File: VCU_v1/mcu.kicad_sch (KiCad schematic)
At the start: 16 parts, among them SW1 SW_Push, U3 STM32H723ZGT6, Y1 16 MHz, Y2 32.768 kHz

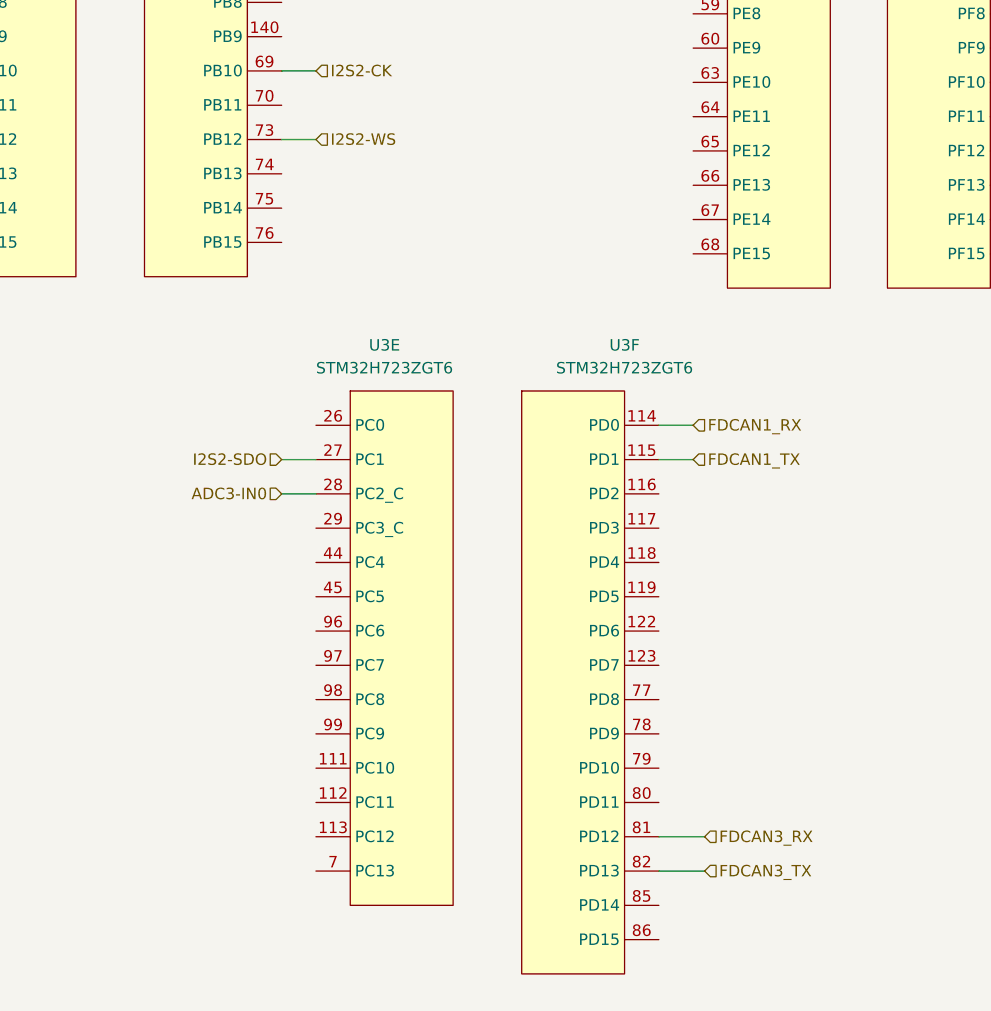
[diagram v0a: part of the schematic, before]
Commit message: added rpp, pedal buffer/low pass, can transceivers, began connector pinout
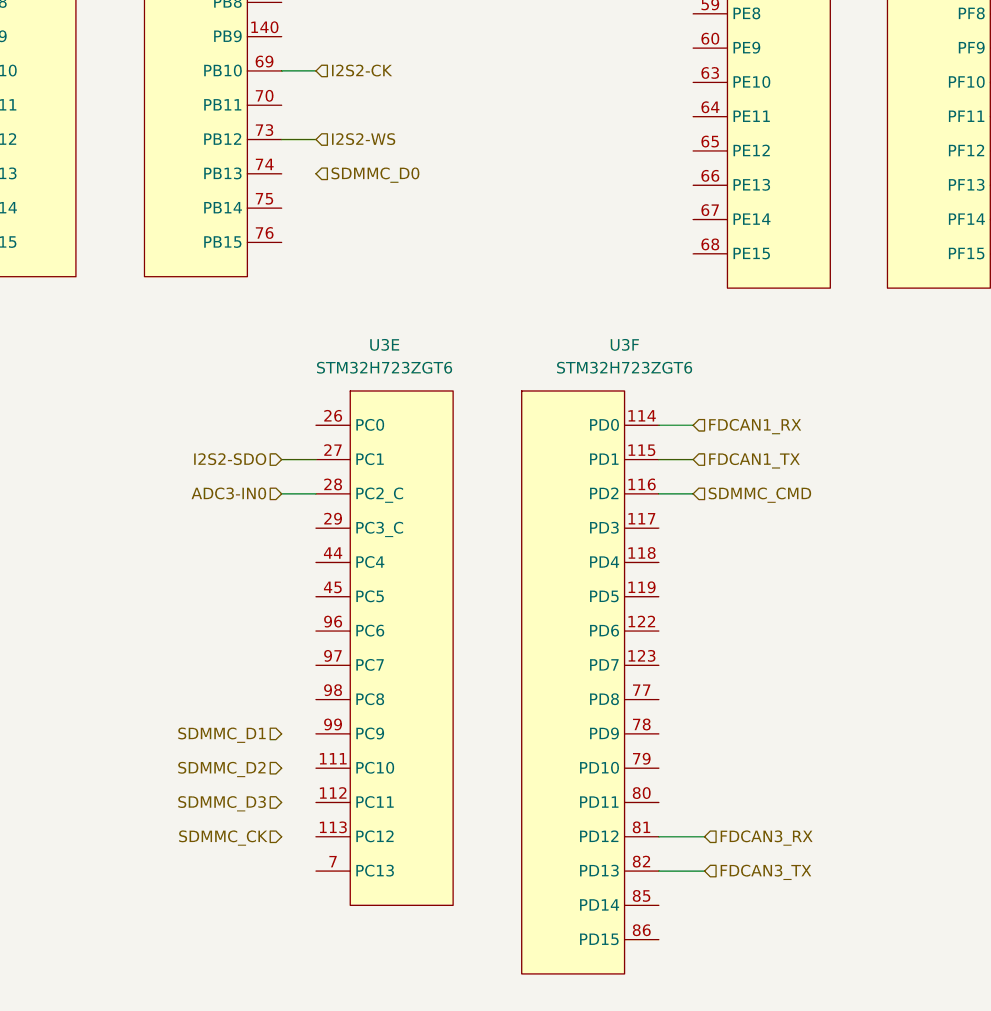
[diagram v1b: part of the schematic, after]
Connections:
- net SDMMC_CMD: now reaches U3.116 (PD2)
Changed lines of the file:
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@@
+	(wire
+		(pts
+			(xy 209.55 110.49) (xy 213.36 110.49)
+		)
+		(stroke
+			(width 0)
+			(type default)
+		)
+	)
 	(wire
 		(pts
@@
 		)
 	)
+	(hierarchical_label "SDMMC_D2"
+		(shape input)
+		(at 167.64 140.97 180)
+		(effects
+			(font
+				(size 1.27 1.27)
+			)
+			(justify right)
+		)
+	)
 	(hierarchical_label "I2S2-SDO"
 		(shape input)
@@
 		)
 	)
+	(hierarchical_label "SDMMC_D0"
+		(shape input)
+		(at 171.45 74.93 0)
+		(effects
+			(font
+				(size 1.27 1.27)
+			)
+			(justify left)
+		)
+	)
 	(hierarchical_label "DEBUG_SWCLK"
 		(shape input)
@@
 		)
 	)
+	(hierarchical_label "SDMMC_D1"
+		(shape input)
+		(at 167.64 137.16 180)
+		(effects
+			(font
+				(size 1.27 1.27)
+			)
+			(justify right)
+		)
+	)
 	(hierarchical_label "DEBUG_SWDIO"
 		(shape input)
@@
 		)
 	)
+	(hierarchical_label "SDMMC_D3"
+		(shape input)
+		(at 167.64 144.78 180)
+		(effects
+			(font
+				(size 1.27 1.27)
+			)
+			(justify right)
+		)
+	)
 	(hierarchical_label "FDCAN1_RX"
 		(shape input)
@@
 		)
 	)
+	(hierarchical_label "SDMMC_CK"
+		(shape input)
+		(at 167.64 148.59 180)
+		(effects
+			(font
+				(size 1.27 1.27)
+			)
+			(justify right)
+		)
+	)
 	(hierarchical_label "I2S2-CK"
 		(shape input)
@@
 		(effects
 			(font
+				(size 1.27 1.27)
+			)
+			(justify left)
+		)
+	)
+	(hierarchical_label "SDMMC_CMD"
+		(shape input)
+		(at 213.36 110.49 0)
+		(effects
+			(font

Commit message: p dih r
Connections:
- net GPIO_IN_E7: now reaches U3.58 (PE7)
- net GPIO_IN_E8: now reaches U3.59 (PE8)
- net GPIO_IN_E9: now reaches U3.60 (PE9)
- net GPIO_OUT_E10: now reaches U3.63 (PE10)
- net GPIO_OUT_E11: now reaches U3.64 (PE11)
- net GPIO_OUT_E12: now reaches U3.65 (PE12)
- net GPIO_OUT_E13: now reaches U3.66 (PE13)
- net GPIO_OUT_E14: now reaches U3.67 (PE14)
- net GPIO_OUT_E15: now reaches U3.68 (PE15)
- net GPIO_IN_F13: now reaches U3.53 (PF13)
- net GPIO_IN_F14: now reaches U3.54 (PF14)
- net GPIO_IN_F15: now reaches U3.55 (PF15)
- net GPIO_IN_G0: now reaches U3.56 (PG0)
- net GPIO_IN_G1: now reaches U3.57 (PG1)

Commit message: left to do before layout: wire DRS/Debug LEDs to connector, add BRUHbus ports
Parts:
- added C62, C69, C70, C71, C72, C73, C74, C75, C76, C77, C78, C79, C80, C81: 100n, Capacitor_SMD:C_0603_1608Metric_Pad1.08x0.95mm_HandSolder, symbol BFR Capacitors:06035C104KAT2A
- added J2: NUCLEO CONNECTOR LEFT, symbol Connector_Generic:Conn_02x35_Odd_Even
- added J3: NUCLEO CONNECTOR RIGHT, symbol Connector_Generic:Conn_02x35_Odd_Even
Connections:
- net +3.3V: now also C62.2, C69.2, C70.2, C71.2, C72.2, C73.2, C74.2, C75.2, C76.2, C77.2, C78.2, C79.2, C80.2, C81.2
- net ADC3-IN0: now also J2.35 (Pin_35)
- net ADC3-IN6: now also J3.42 (Pin_42)
- net ADC3-IN7: now also J2.54 (Pin_54)
- net ADC3-IN8: now also J2.9 (Pin_9)
- net ADC3-IN9: now also J3.38 (Pin_38)
- net DEBUG_SWCLK: now also J2.15 (Pin_15)
- net DEBUG_SWDIO: now also J2.13 (Pin_13)
- net DEBUG_SWO: now also J3.31 (Pin_31)
- net FDCAN1_RX: now also J2.57 (Pin_57)
- net FDCAN1_TX: now also J2.55 (Pin_55)
- net FDCAN2_RX: now also J3.29 (Pin_29)
- net FDCAN2_TX: now also J3.17 (Pin_17)
- net FDCAN3_RX: now also J3.43 (Pin_43)
- net FDCAN3_TX: now also J3.41 (Pin_41)
- net GND: now also C62.1, C69.1, C70.1, C71.1, C72.1, C73.1, C74.1, C75.1, C76.1, C77.1, C78.1, C79.1, C80.1, C81.1, J2.19 (Pin_19), J2.20 (Pin_20), J2.22 (Pin_22), J2.49 (Pin_49), J2.60 (Pin_60), J2.8 (Pin_8), J3.20 (Pin_20), J3.32 (Pin_32), J3.39 (Pin_39), J3.54 (Pin_54), J3.63 (Pin_63), J3.9 (Pin_9)
- net GPIO_IN_E7: now also J3.44 (Pin_44)
- net GPIO_IN_E8: now also J3.40 (Pin_40)
- net GPIO_IN_E9: now also J3.52 (Pin_52)
- net GPIO_IN_F13: now also J3.57 (Pin_57)
- net GPIO_IN_F14: now also J3.50 (Pin_50)
- net GPIO_IN_F15: now also J3.60 (Pin_60)
- net GPIO_IN_G0: now also J2.59 (Pin_59)
- net GPIO_IN_G1: now also J2.58 (Pin_58)
- net GPIO_OUT_E10: now also J3.47 (Pin_47)
- net GPIO_OUT_E11: now also J3.56 (Pin_56)
- net GPIO_OUT_E12: now also J3.49 (Pin_49)
- net GPIO_OUT_E13: now also J3.55 (Pin_55)
- net GPIO_OUT_E14: now also J3.51 (Pin_51)
- net GPIO_OUT_E15: now also J3.53 (Pin_53)
- net I2S2-CK: now also J3.25 (Pin_25)
- net I2S2-SDO: now also J2.36 (Pin_36)
- net I2S2-WS: now also J3.16 (Pin_16)
- net SDMMC_CK: now also U3.113 (PC12), J2.3 (Pin_3)
- net SDMMC_CMD: now also J2.4 (Pin_4)
- net SDMMC_D0: now also U3.74 (PB13), J3.30 (Pin_30)
- net SDMMC_D1: now also U3.99 (PC9), J3.1 (Pin_1)
- net SDMMC_D2: now also U3.111 (PC10), J2.1 (Pin_1)
- net SDMMC_D3: now also U3.112 (PC11), J2.2 (Pin_2)
- net SPI1_MISO: now also J3.13 (Pin_13)
- net SPI1_MOSI: now also J3.15 (Pin_15)
- net SPI1_SCK: now also J3.11 (Pin_11)
- net USB_D+: now also J3.12 (Pin_12)
- net USB_D-: now also J3.14 (Pin_14)
- net PA8: now reaches U3.100 (PA8)
- net PA8: now also J3.23 (Pin_23)
- net PA9: now reaches U3.101 (PA9)
- net PA9: now also J3.21 (Pin_21)
- net PA10: now reaches U3.102 (PA10)
- net PA10: now also J3.33 (Pin_33)
- net PA15: now reaches U3.110 (PA15)
- net PA15: now also J2.17 (Pin_17)
- net TIM2_PWM_CH1: now reaches U3.34 (PA0)
- net TIM2_PWM_CH1: now also J2.28 (Pin_28)
- net TIM2_PWM_CH2: now reaches U3.35 (PA1)
- net TIM2_PWM_CH2: now also J2.30 (Pin_30)
- net TIM2_PWM_CH3: now reaches U3.36 (PA2)
- net TIM2_PWM_CH3: now also J3.35 (Pin_35)
- net PA3: now reaches U3.37 (PA3)
- net PA3: now also J3.37 (Pin_37)
- net PA4: now reaches U3.40 (PA4)
- net PA4: now also J2.32 (Pin_32)
- net PD3: now reaches U3.117 (PD3)
- net PD3: now also J2.40 (Pin_40)
- net PD4: now reaches U3.118 (PD4)
- net PD4: now also J2.39 (Pin_39)
- net PD5: now reaches U3.119 (PD5)
- net PD5: now also J2.41 (Pin_41)
- net PD6: now reaches U3.122 (PD6)
- net PD6: now also J2.43 (Pin_43)
- net PD7: now reaches U3.123 (PD7)
- net PD7: now also J2.45 (Pin_45)
- net PD8: now reaches U3.77 (PD8)
- net PD8: now also J3.10 (Pin_10)
- net PD9: now reaches U3.78 (PD9)
- net PD9: now also J2.69 (Pin_69)
- net PD10: now reaches U3.79 (PD10)
- net PD10: now also J3.65 (Pin_65)
- net PD11: now reaches U3.80 (PD11)
- net PD11: now also J3.45 (Pin_45)
- net PD14: now reaches U3.85 (PD14)
- net PD14: now also J3.46 (Pin_46)
- net PD15: now reaches U3.86 (PD15)
- net PD15: now also J3.48 (Pin_48)
- net PE2: now reaches U3.1 (PE2)
- net PE2: now also J2.46 (Pin_46)
- net PE0: now reaches U3.141 (PE0)
- net PE0: now also J3.64 (Pin_64)
- net PE1: now reaches U3.142 (PE1)
- net PE1: now also J2.61 (Pin_61)
- net PE3: now reaches U3.2 (PE3)
- net PE3: now also J2.47 (Pin_47)
- net PE4: now reaches U3.3 (PE4)
- net PE4: now also J2.48 (Pin_48)
- net PE5: now reaches U3.4 (PE5)
- net PE5: now also J2.50 (Pin_50)
- net PE6: now reaches U3.5 (PE6)
- net PE6: now also J2.62 (Pin_62)
- net VBAT: now reaches BT1.1 (+), U3.6 (VBAT)
- net VBAT: now also J2.33 (Pin_33)
- net PF0: now reaches U3.10 (PF0)
- net PF0: now also J2.53 (Pin_53)
- net PF1: now reaches U3.11 (PF1)
- net PF1: now also J2.51 (Pin_51)
- net PF2: now reaches U3.12 (PF2)
- net PF2: now also J2.52 (Pin_52)
- net PF3: now reaches U3.13 (PF3)
- net PF3: now also J3.58 (Pin_58)
- net PF5: now reaches U3.15 (PF5)
- net PF5: now also J3.36 (Pin_36)
- net PF7: now reaches U3.19 (PF7)
- net PF7: now also J2.11 (Pin_11)
- net PF9: now reaches U3.21 (PF9)
- net PF9: now also J2.56 (Pin_56)
- net PF11: now reaches U3.49 (PF11)
- net PF11: now also J3.62 (Pin_62)
- net PF12: now reaches U3.50 (PF12)
- net PF12: now also J3.59 (Pin_59)
- net PC0: now reaches U3.26 (PC0)
- net PC0: now also J2.38 (Pin_38)
- net PC3: now reaches U3.29 (PC3_C)
- net PC3: now also J2.37 (Pin_37)
- net PC4: now reaches U3.44 (PC4)
- net PC4: now also J3.34 (Pin_34)
- net PC5: now reaches U3.45 (PC5)
- net PC5: now also J3.6 (Pin_6)
- net PC13: now reaches U3.7 (PC13)
- net PC13: now also J2.23 (Pin_23)
- net PC6: now reaches U3.96 (PC6)
- net PC6: now also J3.4 (Pin_4)
- net PC7: now reaches U3.97 (PC7)
- net PC7: now also J3.19 (Pin_19)
- net PC8: now reaches U3.98 (PC8)
- net PC8: now also J3.2 (Pin_2)
- net PB4: now reaches U3.134 (PB4)
- net PB4: now also J3.27 (Pin_27)
- net PB7: now reaches U3.137 (PB7)
- net PB7: now also J2.21 (Pin_21)
- net PB8: now reaches U3.139 (PB8)
- net PB8: now also J3.3 (Pin_3)
- net PB9: now reaches U3.140 (PB9)
- net PB9: now also J3.5 (Pin_5)
- net PB0: now reaches U3.46 (PB0)
- net PB0: now also J2.34 (Pin_34)
- net PB1: now reaches U3.47 (PB1)
- net PB1: now also J3.24 (Pin_24)
- net PB2: now reaches U3.48 (PB2)
- net PB2: now also J3.22 (Pin_22)
- net PB11: now reaches U3.70 (PB11)
- net PB11: now also J3.18 (Pin_18)
- net PB14: now reaches U3.75 (PB14)
- net PB14: now also J3.28 (Pin_28)
- net TIM12_PWM_CH2: now reaches U3.76 (PB15)
- net TIM12_PWM_CH2: now also J3.26 (Pin_26)
- net GPIO_G9: now reaches U3.124 (PG9)
- net GPIO_G9: now also J2.63 (Pin_63)
- net GPIO_G10: now reaches U3.125 (PG10)
- net GPIO_G10: now also J2.66 (Pin_66)
- net GPIO_G11: now reaches U3.126 (PG11)
- net GPIO_G11: now also J2.70 (Pin_70)
- net GPIO_G12: now reaches U3.127 (PG12)
- net GPIO_G12: now also J2.65 (Pin_65)
- net GPIO_G13: now reaches U3.128 (PG13)
- net GPIO_G13: now also J2.68 (Pin_68)
- net GPIO_G14: now reaches U3.129 (PG14)
- net GPIO_G14: now also J3.61 (Pin_61)
- net GPIO_G15: now reaches U3.132 (PG15)
- net GPIO_G15: now also J2.64 (Pin_64)
- net GPIO_G2: now reaches U3.87 (PG2)
- net GPIO_G2: now also J2.42 (Pin_42)
- net GPIO_G3: now reaches U3.88 (PG3)
- net GPIO_G3: now also J2.44 (Pin_44)
- net GPIO_G4: now reaches U3.89 (PG4)
- net GPIO_G4: now also J3.69 (Pin_69)
- net GPIO_G5: now reaches U3.90 (PG5)
- net GPIO_G5: now also J3.68 (Pin_68)
- net GPIO_G6: now reaches U3.91 (PG6)
- net GPIO_G6: now also J3.70 (Pin_70)
- net GPIO_G7: now reaches U3.92 (PG7)
- net GPIO_G7: now also J3.67 (Pin_67)
- net GPIO_G8: now reaches U3.93 (PG8)
- net GPIO_G8: now also J3.66 (Pin_66)
- new net +5V: J2.6 (Pin_6)
- new net PC14: J2.25 (Pin_25)
- new net PC15: J2.27 (Pin_27)
- no-connect marks 1 -> 15
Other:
- note added: "<- 3V3"
- note added: "<- 5V"
- note added: "<- 5V USB STLK"
- note added: "<- IOREF"
- note added: "<- NRST"
- note added: "<- VIN"
- note added: "BOOT0 ->"
- note added: "Nucleo Headers"
- note added: "PH0 ->"
- note added: "PH1 ->"
- note added: "VDD ->"
- note added: "VREFP ->"
- note added: "heinous layout T-T but one 100nF cap for each VDD pin"
- moved on the sheet: BT1, C10, C11, C12, C13, C14, C15, C16, C17, JP1, R4, R5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

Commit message: v1 schematic (actually) complete, let the layout commence
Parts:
- added TP7, TP8, TP9: RH-5015, TestPoint:TestPoint_Keystone_5015_Micro_Mini, symbol .Test-Point:RH-5015
- BT1: footprint (none) -> SMTU2032-C:Untitled; Mouser P/N (none) -> 614-SMTU2032-C; P/N (none) -> SMTU2032-C
- J2, J3: footprint (none) -> Connector_PinHeader_2.54mm:PinHeader_2x35_P2.54mm_Vertical
- JP1: footprint (none) -> Connector_PinHeader_2.54mm:PinHeader_1x03_P2.54mm_Vertical
- SW1: footprint (none) -> Button_Switch_SMD:SW_Push_1P1T_NO_CK_KMR2; Mouser P/N (none) -> 611-KMR231NG LFS; P/N (none) -> KMR231NG LFS
- Y1: footprint (none) -> ECS-160-18-28X-AEN-TR :Untitled
- Y2: footprint (none) -> ECS-.327-7-1210B-N-TR:Untitled
- renumbered C11 to C18, C80 to C19, C81 to C20, C69 to C21, C70 to C22, C62 to C23, C71 to C24, C72 to C25, C73 to C26, C74 to C27, C75 to C28, C76 to C29, C77 to C30, C78 to C31, C79 to C32, C10 to C33, C12 to C34, C13 to C35, C15 to C36, C16 to C37, C17 to C38, C14 to C39, R5 to R10, R4 to R9, U3 to U5
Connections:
- net I2S2-CK: now also TP7.1
- net I2S2-SDO: now also TP9.1
- net I2S2-WS: now also TP8.1

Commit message: begin pcb design
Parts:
- Y1: footprint ECS-160-18-28X-AEN-TR :Untitled -> ECS-160-18-28X-AEN-TR:Untitled
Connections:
- net GPIO_OUT_E10 renamed GPIO_E10
- net GPIO_OUT_E11 renamed GPIO_E11
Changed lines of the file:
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@@
 	(wire
 		(pts
-			(xy 26.67 242.57) (xy 25.4 242.57)
-		)
-		(stroke
-			(width 0)
-			(type default)
-		)
-	)
-	(wire
-		(pts
 			(xy 322.58 146.05) (xy 326.39 146.05)
 		)
@@
 	(wire
 		(pts
-			(xy 26.67 236.22) (xy 25.4 236.22)
-		)
-		(stroke
-			(width 0)
-			(type default)
-		)
-	)
-	(wire
-		(pts
 			(xy 214.63 74.93) (xy 220.98 74.93)
 		)
@@
 		)
 	)
-	(hierarchical_label "GPIO_OUT_E10"
-		(shape input)
-		(at 316.23 76.2 180)
-		(effects
-			(font
-				(size 1.27 1.27)
-			)
-			(justify right)
-		)
-	)
 	(hierarchical_label "DEBUG_SWO"
 		(shape input)
@@
 		)
 	)
+	(hierarchical_label "GPIO_E10"
+		(shape input)
+		(at 316.23 76.2 180)
+		(effects
+			(font
+				(size 1.27 1.27)
+			)
+			(justify right)
+		)
+	)
 	(hierarchical_label "GPIO_G10"
 		(shape input)
@@
 		)
 	)
-	(hierarchical_label "GPIO_OUT_E11"
-		(shape input)
-		(at 316.23 80.01 180)
-		(effects
-			(font
-				(size 1.27 1.27)
-			)
-			(justify right)
-		)
-	)
 	(hierarchical_label "GPIO_G6"
 		(shape input)
@@
 		)
 	)
+	(hierarchical_label "GPIO_E11"
+		(shape input)
+		(at 316.23 80.01 180)
+		(effects
+			(font
+				(size 1.27 1.27)
+			)
+			(justify right)
+		)
+	)
 	(hierarchical_label "ADC3-IN7"
 		(shape input)
@@
 			)
 		)
-		(property "Footprint" "ECS-160-18-28X-AEN-TR :Untitled"
+		(property "Footprint" "ECS-160-18-28X-AEN-TR:Untitled"
 			(at 38.1 236.22 0)
 			(effects
